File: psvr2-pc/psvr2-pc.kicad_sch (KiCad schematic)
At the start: 91 parts, among them IC1 SN65MLVD200A, IC2 SN65MLVD200A, J1 USB_C_Receptacle, J2 USB3_B_Micro, J3 DP_47272, J4 Barrel_Jack_Switch, J5 Conn_01x02_Pin, Q1 Si2301CDS, Q2 PN2222A, Q3 Si2301CDS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

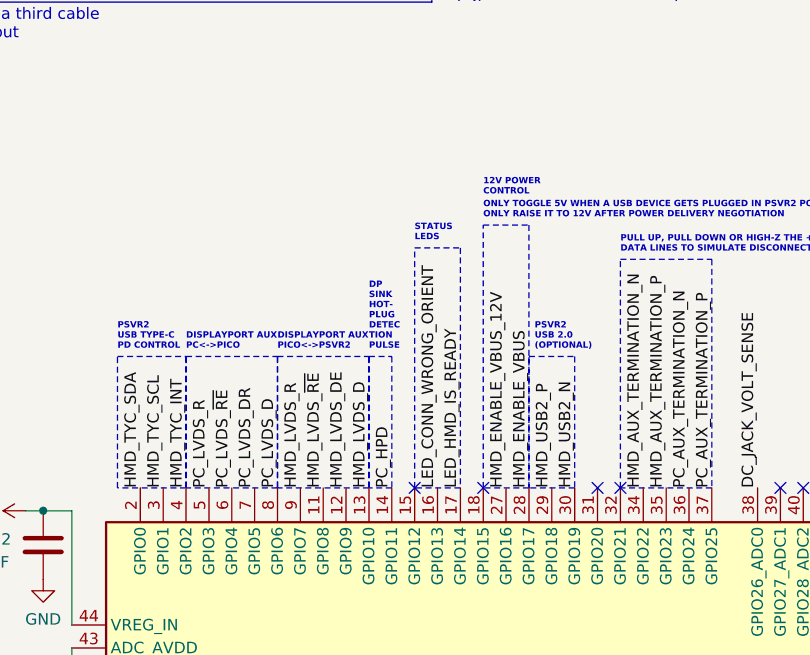
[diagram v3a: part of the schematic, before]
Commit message: Add two additional testpoints to tap any posible hardware RP2040 UART0 signals from GPIO12/13, as requested by iVRy. Change the LED pins slightly to make room.
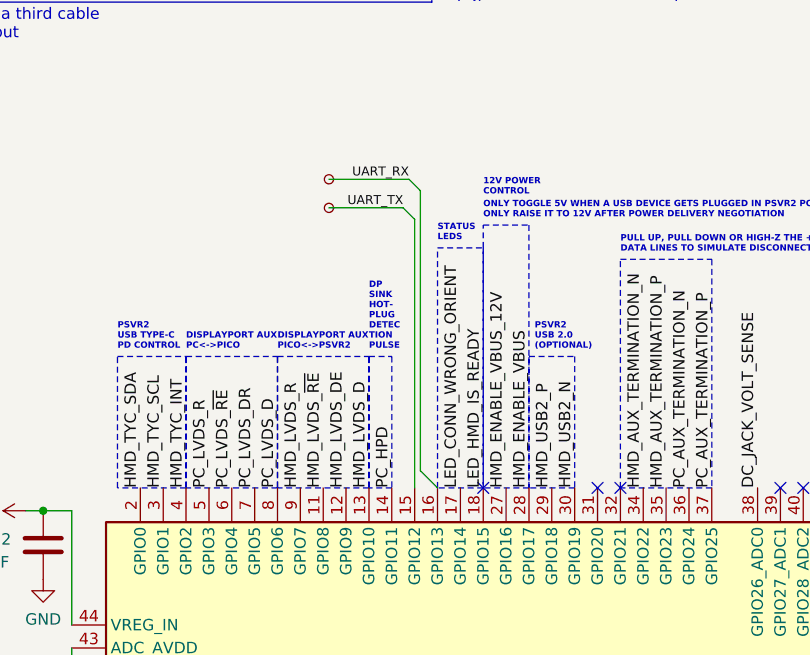
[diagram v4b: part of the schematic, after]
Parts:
- added TP1, TP2: TestPoint_Small, TestPoint:TestPoint_Pad_D2.5mm, symbol Connector:TestPoint_Small
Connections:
- net LED_CONN_WRONG_ORIENT: now also U1.17 (GPIO14); no longer U1.16 (GPIO13)
- net LED_HMD_IS_READY: now also U1.18 (GPIO15); no longer U1.17 (GPIO14)
- net UART_TX: now reaches U1.15 (GPIO12)
- net UART_TX: now also TP1.1
- new net UART_RX: TP2.1, U1.16 (GPIO13)
- no-connect marks 17 -> 16
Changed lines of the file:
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@@
   (no_connect (at 41.91 27.94))
   (no_connect (at 211.455 149.225))
-  (no_connect (at 170.815 149.225))
   (no_connect (at 140.335 200.025))
   (no_connect (at 41.91 20.32))
@@
     (stroke (width 0) (type default))
   )
+  (wire (pts (xy 171.45 116.205) (xy 170.18 114.935))
+    (stroke (width 0) (type default))
+  )
   (wire (pts (xy 311.785 164.465) (xy 311.785 161.29))
     (stroke (width 0) (type default))
@@
     (stroke (width 0) (type default))
   )
+  (wire (pts (xy 171.45 147.32) (xy 171.45 116.205))
+    (stroke (width 0) (type default))
+  )
   (wire (pts (xy 300.355 153.67) (xy 295.275 153.67))
     (stroke (width 0) (type default))
@@
     (stroke (width 0) (type default))
   )
+  (wire (pts (xy 169.545 118.11) (xy 161.29 118.11))
+    (stroke (width 0) (type default))
+  )
   (wire (pts (xy 150.495 207.645) (xy 138.43 207.645))
     (stroke (width 0) (type default))
@@
     (stroke (width 0) (type default))
   )
+  (wire (pts (xy 161.29 114.935) (xy 170.18 114.935))
+    (stroke (width 0) (type default))
+  )
   (wire (pts (xy 194.31 211.455) (xy 194.31 217.17))
     (stroke (width 0) (type default))
@@
     (stroke (width 0) (type default))
   )
+  (wire (pts (xy 170.815 119.38) (xy 170.815 149.225))
+    (stroke (width 0) (type default))
+  )
   (wire (pts (xy 380.365 206.375) (xy 380.365 205.74))
     (stroke (width 0) (type default))
@@
     (stroke (width 0) (type default))
   )
+  (wire (pts (xy 171.45 147.32) (xy 173.355 149.225))
+    (stroke (width 0) (type default))
+  )
   (wire (pts (xy 216.535 200.025) (xy 222.885 200.025))
     (stroke (width 0) (type default))
@@
     (stroke (width 0) (type default))
   )
+  (wire (pts (xy 170.815 119.38) (xy 169.545 118.11))
+    (stroke (width 0) (type default))
+  )
   (wire (pts (xy 329.565 213.36) (xy 326.39 213.36))
     (stroke (width 0) (type default))
@@
     (fill (type none))
   )
-  (rectangle (start 170.815 122.555) (end 175.895 149.225)
+  (rectangle (start 173.355 122.555) (end 178.435 149.225)
     (stroke (width 0) (type dot))
     (fill (type none))
@@
     (effects (font (face "Courier New") (size 1.27 1.27) (thickness 0.254) bold italic) (justify left bottom))
   )
-  (text "STATUS\nLEDS" (at 170.815 121.92 0)
+  (text "STATUS\nLEDS" (at 173.355 121.92 0)
     (effects (font (size 0.7 0.7) bold) (justify left bottom))
   )
@@
     (effects (font (size 1.27 1.27)) (justify right bottom))
   )
+  (label "LED_HMD_IS_READY" (at 178.435 149.225 90) (fields_autoplaced)
+    (effects (font (size 1.27 1.27)) (justify left bottom))
+  )
   (label "PC_AUX_N" (at 240.03 116.84 180) (fields_autoplaced)
     (effects (font (size 1.27 1.27)) (justify right bottom))
@@
     (effects (font (size 1.27 1.27)) (justify left bottom))
   )
+  (label "UART_RX" (at 170.18 114.935 180) (fields_autoplaced)
+    (effects (font (size 1 1)) (justify right bottom))
+  )
   (label "HMD_AUX_TERMINATION_N" (at 196.215 149.225 90) (fields_autoplaced)
     (effects (font (size 1.27 1.27)) (justify left bottom))
@@
     (effects (font (size 1.27 1.27)) (justify left bottom))
   )
-  (label "LED_CONN_WRONG_ORIENT" (at 173.355 149.225 90) (fields_autoplaced)
-    (effects (font (size 1.27 1.27)) (justify left bottom))
-  )
   (label "PC_LVDS_DR" (at 381 154.94 0) (fields_autoplaced)
     (effects (font (size 1.27 1.27)) (justify left bottom))
@@
     (effects (font (size 1.27 1.27)) (justify right bottom))
   )
+  (label "LED_CONN_WRONG_ORIENT" (at 175.895 149.225 90) (fields_autoplaced)
+    (effects (font (size 1.27 1.27)) (justify left bottom))
+  )
   (label "HMD_TYC_SDA" (at 195.58 41.91 0) (fields_autoplaced)
     (effects (font (size 1.27 1.27)) (justify left bottom))
@@
     (effects (font (size 1.27 1.27)) (justify left bottom))
   )
-  (label "LED_HMD_IS_READY" (at 175.895 149.225 90) (fields_autoplaced)
-    (effects (font (size 1.27 1.27)) (justify left bottom))
-  )
   (label "PC_USB2_P" (at 116.205 205.105 0) (fields_autoplaced)
     (effects (font (size 1.27 1.27)) (justify left bottom))
@@
     (effects (font (size 1.27 1.27)) (justify left bottom))
   )
+  (label "UART_TX" (at 169.545 118.11 180) (fields_autoplaced)
+    (effects (font (size 1 1)) (justify right bottom))
+  )
   (label "SWCLK" (at 206.375 200.025 180) (fields_autoplaced)
     (effects (font (size 1 1)) (justify right bottom))
@@
     )
   )
+  (symbol (lib_id "Connector:TestPoint_Small") (at 161.29 118.11 0) (mirror x) (unit 1)
+    (in_bom yes) (on_board yes) (dnp no) (fields_autoplaced)
+    (property "Reference" "TP1" (at 162.56 119.38 0)
+      (effects (font (size 1.27 1.27)) (justify left) hide)
+    )
+    (property "Value" "TestPoint_Small" (at 162.56 116.84 0)
+      (effects (font (size 1.27 1.27)) (justify left) hide)
+    )
+    (property "Footprint" "TestPoint:TestPoint_Pad_D2.5mm" (at 166.37 118.11 0)
+      (effects (font (size 1.27 1.27)) hide)
+    )
+    (property "Datasheet" "~" (at 166.37 118.11 0)
+      (effects (font (size 1.27 1.27)) hide)
+    )
+    (pin "1")
+    (instances
+      (project "psvr2-pc"
+        (path "/381748c8-fb8a-4e0a-a26e-44fd86369b77"
+          (reference "TP1") (unit 1)
+        )
+      )
+    )
+  )
   (symbol (lib_id "Device:R") (at 389.89 200.66 0) (unit 1)
     (in_bom yes) (on_board yes) (dnp no) (fields_autoplaced)
@@
         )
       )
+    )
+  )
+  (symbol (lib_id "Connector:TestPoint_Small") (at 161.29 114.935 0) (mirror x) (unit 1)
+    (in_bom yes) (on_board yes) (dnp no) (fields_autoplaced)
+    (property "Reference" "TP2" (at 162.56 116.205 0)
+      (effects (font (size 1.27 1.27)) (justify left) hide)
+    )
+    (property "Value" "TestPoint_Small" (at 162.56 113.665 0)
+      (effects (font (size 1.27 1.27)) (justify left) hide)
+    )
+    (property "Footprint" "TestPoint:TestPoint_Pad_D2.5mm" (at 166.37 114.935 0)
+      (effects (font (size 1.27 1.27)) hide)
+    )
+    (property "Datasheet" "~" (at 166.37 114.935 0)
+      (effects (font (size 1.27 1.27)) hide)
+    )
+    (pin "1")
+    (instances
+      (project "psvr2-pc"
+        (path "/381748c8-fb8a-4e0a-a26e-44fd86369b77"
+          (reference "TP2") (unit 1)
+        )
+      )

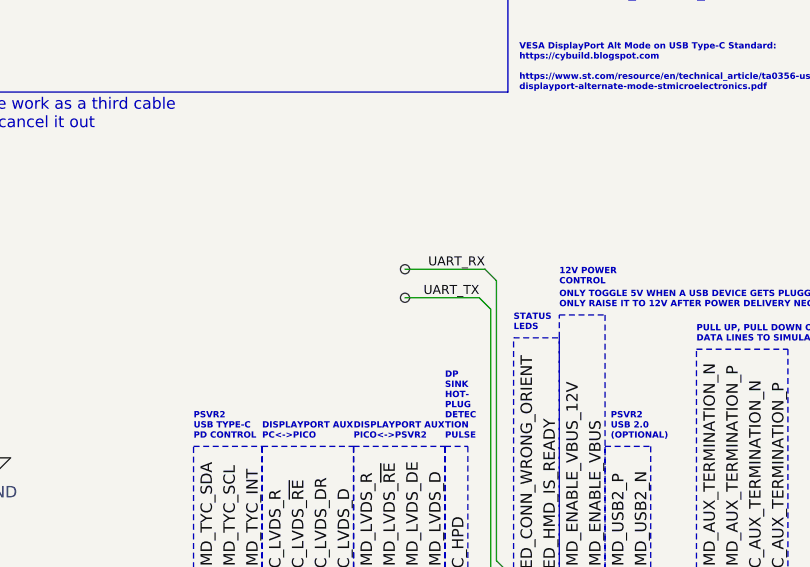
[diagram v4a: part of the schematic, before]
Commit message: Remove the UART testpoints from the bill of materials. Adjust the penguin layer masks to line up a bit better.
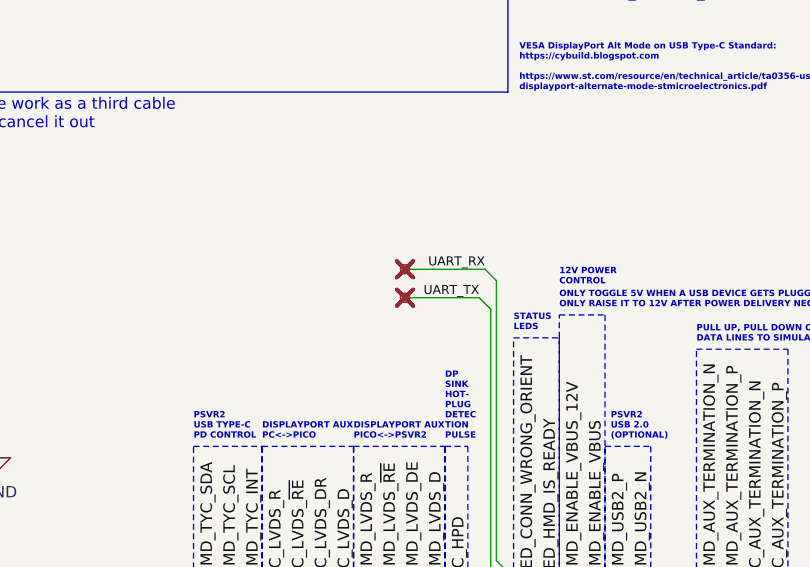
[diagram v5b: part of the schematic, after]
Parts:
- TP1, TP2: now not fitted; now left out of the parts list
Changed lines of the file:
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@@
   )
   (symbol (lib_id "Connector:TestPoint_Small") (at 161.29 118.11 0) (mirror x) (unit 1)
-    (in_bom yes) (on_board yes) (dnp no) (fields_autoplaced)
+    (in_bom no) (on_board yes) (dnp yes) (fields_autoplaced)
     (property "Reference" "TP1" (at 162.56 119.38 0)
       (effects (font (size 1.27 1.27)) (justify left) hide)
@@
   )
   (symbol (lib_id "Connector:TestPoint_Small") (at 161.29 114.935 0) (mirror x) (unit 1)
-    (in_bom yes) (on_board yes) (dnp no) (fields_autoplaced)
+    (in_bom no) (on_board yes) (dnp yes) (fields_autoplaced)
     (property "Reference" "TP2" (at 162.56 116.205 0)
       (effects (font (size 1.27 1.27)) (justify left) hide)

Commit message: Switch the footprint of the 100uF capacitors from 0805 to 1206. As those are listed as "basic", unfortunately making the layout more cluttered and ugly, for now.
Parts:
- C10, C11, C15, C16, C17, C18: footprint Capacitor_SMD:C_0805_2012Metric -> Capacitor_SMD:C_1206_3216Metric
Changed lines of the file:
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@@
       (effects (font (size 1.27 1.27)) (justify right))
     )
-    (property "Footprint" "Capacitor_SMD:C_0805_2012Metric" (at 104.775 133.6548 0)
+    (property "Footprint" "Capacitor_SMD:C_1206_3216Metric" (at 104.775 133.6548 0)
       (effects (font (size 1.27 1.27)) hide)
     )
@@
       (effects (font (size 1.27 1.27)) (justify right))
     )
-    (property "Footprint" "Capacitor_SMD:C_0805_2012Metric" (at 104.775 140.0048 0)
+    (property "Footprint" "Capacitor_SMD:C_1206_3216Metric" (at 104.775 140.0048 0)
       (effects (font (size 1.27 1.27)) hide)
     )
@@
       (effects (font (size 1.27 1.27)) (justify left))
     )
-    (property "Footprint" "Capacitor_SMD:C_0805_2012Metric" (at 110.7948 186.055 0)
+    (property "Footprint" "Capacitor_SMD:C_1206_3216Metric" (at 110.7948 186.055 0)
       (effects (font (size 1.27 1.27)) hide)
     )
@@
       (effects (font (size 1.27 1.27)) (justify right))
     )
-    (property "Footprint" "Capacitor_SMD:C_0805_2012Metric" (at 104.775 152.7048 0)
+    (property "Footprint" "Capacitor_SMD:C_1206_3216Metric" (at 104.775 152.7048 0)
       (effects (font (size 1.27 1.27)) hide)
     )
@@
       (effects (font (size 1.27 1.27)) (justify right))
     )
-    (property "Footprint" "Capacitor_SMD:C_0805_2012Metric" (at 104.775 146.3548 0)
+    (property "Footprint" "Capacitor_SMD:C_1206_3216Metric" (at 104.775 146.3548 0)
       (effects (font (size 1.27 1.27)) hide)
     )
@@
       (effects (font (size 1.27 1.27)) (justify left))
     )
-    (property "Footprint" "Capacitor_SMD:C_0805_2012Metric" (at 116.5098 186.055 0)
-      (effects (font (size 1.27 1.27)) hide)
-    )
+    (property "Footprint" "Capacitor_SMD:C_1206_3216Metric" (at 116.5098 186.055 0)
+      (effects (font (size 1.27 1.27)) hide)
+    )

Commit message: More resistor adjustments to fit the real-life requirements of cheap components. Add two resistors in series to approximate the right current value in LEDs. Not happy with this, but what are you going to do. Change the 27R to a 33R for the USB termination resistors, hopefully it won't be a problem.
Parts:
- added R27: 51, Resistor_SMD:R_0805_2012Metric, symbol Device:R
- added R39: 10, Resistor_SMD:R_0805_2012Metric, symbol Device:R
- D1: value SS14 -> 1N5819WS; footprint Diode_SMD:D_0805_2012Metric -> Diode_SMD:D_SOD-323; LCSC Part # (none) -> C191023; Mfr. Part # (none) -> 1N5819WS
- R1, R2: value 27R -> 33R
- R19: value 82 -> 33
- R20: value 68 -> 51
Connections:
- net LED_CONN_WRONG_ORIENT: now also R27.2; no longer R19.2
- net at D8.2 (A): now also R39.1; no longer R20.1
- new net: R20.1, R39.2
- new net: R19.2, R27.1
- no-connect marks 16 -> 15
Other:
- note added: "swy: ideally 27Ω, but those aren't JLC basic parts. Closest are 22Ω and 33Ω."
- moved on the sheet: R19, R20

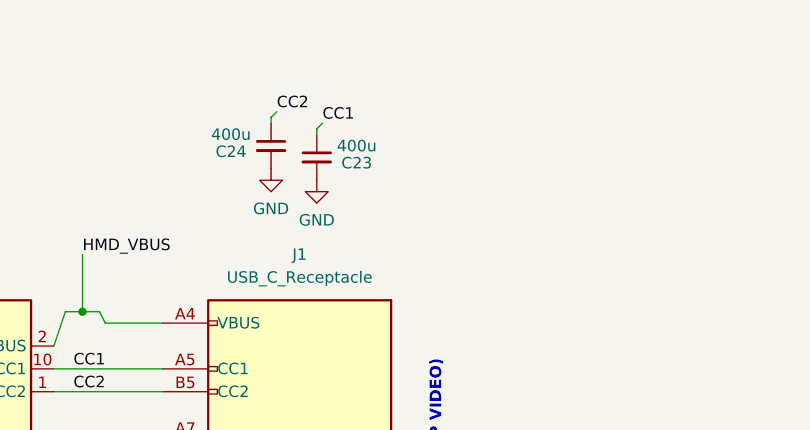
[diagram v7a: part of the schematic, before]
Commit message: Change a few components to make them manufacturable at the lowest cost (basic ones). Change some footprints, add attributes to compensate for the wrong rotation and offset in many parts. Change a capacitor from 400pF to 470pF.
DC 12 jack notes for the top-left cursor position:positions
bad/before: 15.81, -58.9
good/after: 12.83,-61.39

>>> 12.83-15.81
-2.9800000000000004
>>> -61.39--58.9
-2.490000000000002
>>>
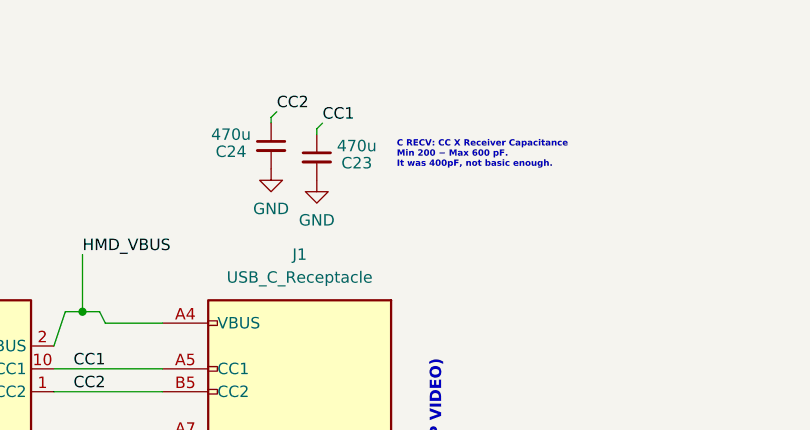
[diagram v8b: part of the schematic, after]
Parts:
- C23, C24: value 400u -> 470u; Field4 (none) -> C13967
- D1, D7, D8, D9: JLCPCB Rotation Offset (none) -> 0
- IC1, IC2, U2, U3: JLCPCB Rotation Offset (none) -> -90
- J4: JLCPCB Position Offset (none) -> -3,-2.5
- Q1, Q2, Q3, Q4, Q5, Q6, Q7, U5: JLCPCB Rotation Offset (none) -> 180
- R13, R14: footprint Resistor_SMD:R_0805_2012Metric -> Resistor_SMD:R_1206_3216Metric
- R25: LCSC Part # (none) -> C17818
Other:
- note added: "C RECV: CC X Receiver Capacitance Min 200 − Max 600 pF. It was 400pF, not basic enough."
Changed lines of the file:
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@@
     (effects (font (size 0.7 0.7) (thickness 0.14) bold) (justify left bottom))
   )
+  (text "C RECV: CC X Receiver Capacitance\nMin 200 − Max 600 pF.\nIt was 400pF, not basic enough."
+    (at 278.765 22.225 0)
+    (effects (font (size 0.7 0.7) (thickness 0.14) bold) (justify left bottom))
+  )
   (text "DP\nSINK\nHOT-\nPLUG\nDETEC\nTION\nPULSE" (at 165.735 133.985 0)
     (effects (font (size 0.7 0.7) bold) (justify left bottom))
@@
       (effects (font (size 1.27 1.27)) hide)
     )
+    (property "JLCPCB Position Offset" "-3,-2.5" (at 24.765 140.97 0)
+      (effects (font (size 1.27 1.27)) hide)
+    )
     (pin "MP")
     (pin "1")
@@
       (effects (font (size 1.27 1.27)) hide)
     )
+    (property "JLCPCB Rotation Offset" "180" (at 46.355 203.2 90)
+      (effects (font (size 1.27 1.27)) hide)
+    )
     (pin "1")
     (pin "2")
@@
       (effects (font (size 1.27 1.27)))
     )
-    (property "Value" "400u" (at 274.32 19.685 0)
+    (property "Value" "470u" (at 274.32 19.685 0)
       (effects (font (size 1.27 1.27)))
     )
@@
       (effects (font (size 1.27 1.27)) hide)
     )
+    (property "Field4" "C13967" (at 269.875 20.955 0)
+      (effects (font (size 1.27 1.27)) hide)
+    )
     (pin "1")
     (pin "2")
@@
       (effects (font (size 1.27 1.27) italic))
     )
+    (property "JLCPCB Rotation Offset" "-90" (at 227.965 44.45 0)
+      (effects (font (size 1.27 1.27)) hide)
+    )
     (pin "8")
     (pin "15")
@@
       (effects (font (size 1.27 1.27)) hide)
     )
+    (property "JLCPCB Rotation Offset" "-90" (at 377.19 149.86 0)
+      (effects (font (size 1.27 1.27)) hide)
+    )
     (pin "8")
     (pin "3")
@@
       (effects (font (size 1.27 1.27)) hide)
     )
+    (property "JLCPCB Rotation Offset" "180" (at 60.96 233.045 0)
+      (effects (font (size 1.27 1.27)) hide)
+    )
     (pin "2")
     (pin "3")
@@
       (effects (font (size 1.27 1.27)) hide)
     )
+    (property "JLCPCB Rotation Offset" "180" (at 46.99 140.97 90)
+      (effects (font (size 1.27 1.27)) hide)
+    )
     (pin "3")
     (pin "2")
@@
       (effects (font (size 1.27 1.27)) hide)
     )
+    (property "JLCPCB Rotation Offset" "180" (at 55.245 175.26 0)
+      (effects (font (size 1.27 1.27)) hide)
+    )
     (pin "3")
     (pin "1")
@@
       (effects (font (size 1.27 1.27)) hide)
     )
+    (property "JLCPCB Rotation Offset" "0" (at 359.41 23.495 0)
+      (effects (font (size 1.27 1.27)) hide)
+    )
     (pin "1")
     (pin "2")
@@
       (effects (font (size 1.27 1.27)) (justify left))
     )
-    (property "Footprint" "Resistor_SMD:R_0805_2012Metric" (at 347.218 194.31 90)
+    (property "Footprint" "Resistor_SMD:R_1206_3216Metric" (at 347.218 194.31 90)
       (effects (font (size 1.27 1.27)) hide)
     )
@@
       (effects (font (size 1.27 1.27)) hide)
     )
+    (property "JLCPCB Rotation Offset" "-90" (at 165.735 248.92 0)
+      (effects (font (size 1.27 1.27)) hide)
+    )
     (pin "1")
     (pin "2")
@@
       (effects (font (size 1.27 1.27)) hide)
     )
+    (property "JLCPCB Rotation Offset" "180" (at 367.665 78.74 0)
+      (effects (font (size 1.27 1.27)) hide)
+    )
     (pin "3")
     (pin "1")
@@
       (effects (font (size 1.27 1.27)) hide)
     )
+    (property "LCSC Part #" "C17818" (at 64.135 149.86 90)
+      (effects (font (size 1.27 1.27)) hide)
+    )
     (pin "1")
     (pin "2")
@@
       (effects (font (size 1.27 1.27)) hide)
     )
+    (property "JLCPCB Rotation Offset" "180" (at 40.64 170.18 0)
+      (effects (font (size 1.27 1.27)) hide)
+    )
     (pin "2")
     (pin "3")
@@
       (effects (font (size 1.27 1.27)) hide)
     )
+    (property "JLCPCB Rotation Offset" "0" (at 44.45 85.09 0)
+      (effects (font (size 1.27 1.27)) hide)
+    )
     (pin "1")
     (pin "2")
@@
       (effects (font (size 1.27 1.27)) hide)
     )
+    (property "JLCPCB Rotation Offset" "180" (at 75.565 238.125 0)
+      (effects (font (size 1.27 1.27)) hide)
+    )
     (pin "3")
     (pin "1")
@@
       (effects (font (size 1.27 1.27)))
     )
-    (property "Value" "400u" (at 260.35 18.415 0)
+    (property "Value" "470u" (at 260.35 18.415 0)
       (effects (font (size 1.27 1.27)))
     )
@@
       (effects (font (size 1.27 1.27)) hide)
     )
+    (property "Field4" "C13967" (at 264.795 19.685 0)
+      (effects (font (size 1.27 1.27)) hide)
+    )
     (pin "1")
     (pin "2")
@@
       (effects (font (size 1.27 1.27)) hide)
     )
+    (property "JLCPCB Rotation Offset" "-90" (at 288.925 201.93 0)
+      (effects (font (size 1.27 1.27)) hide)
+    )
     (pin "8")
     (pin "3")
@@
       (effects (font (size 1.27 1.27)) hide)
     )
+    (property "JLCPCB Rotation Offset" "180" (at 46.355 215.265 90)
+      (effects (font (size 1.27 1.27)) hide)
+    )
     (pin "1")
     (pin "2")
@@
       (effects (font (size 1.27 1.27)) hide)
     )
+    (property "JLCPCB Rotation Offset" "0" (at 359.41 49.53 0)
+      (effects (font (size 1.27 1.27)) hide)
+    )
     (pin "1")
     (pin "2")
@@
       (effects (font (size 1.27 1.27)) hide)
     )
+    (property "JLCPCB Rotation Offset" "0" (at 359.41 36.195 0)
+      (effects (font (size 1.27 1.27)) hide)
+    )
     (pin "1")
     (pin "2")
@@
       (effects (font (size 1.27 1.27)) (justify left))
     )
-    (property "Footprint" "Resistor_SMD:R_0805_2012Metric" (at 347.218 217.17 90)
+    (property "Footprint" "Resistor_SMD:R_1206_3216Metric" (at 347.218 217.17 90)
       (effects (font (size 1.27 1.27)) hide)
     )
